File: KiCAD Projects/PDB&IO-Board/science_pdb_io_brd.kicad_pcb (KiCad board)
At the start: 2 copper layers, 124 x 94.6 mm, 40 parts, among them P11 ENCODER_1, P13 LIMIT1_IN, P14 LIMIT2_IN, P15 LIMIT3_IN, P16 ENCODER_3, P17 MOTOR1_PWM, P18 MOTOR2_PWM, P19 MOTOR3_PWM, P2 RPI_HEADER, P20 MOTOR4_PWM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

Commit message: Progress on Main Board
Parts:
- C4: moved to F.Cu
- U1: footprint Housings_SOIC:SOIC-14_3.9x8.7mm_Pitch1.27mm -> Housings_DIP:DIP-14_W7.62mm
- moved R16 104.8 mm to (181.6, 58.4)
- moved D2 104.8 mm to (181.6, 66.0)
- moved D3 104.8 mm to (194.3, 66.0)
- moved R17 104.8 mm to (194.3, 58.4)
- moved P5 72.4 mm to (119.4, 106.7)
- moved P6 72.4 mm to (139.7, 109.2)
- moved P7 72.4 mm to (129.5, 104.1)
- moved P2 70.0 mm to (174.0, 98.4)
- moved P17 55.3 mm to (108.0, 109.2), turned to 90 degrees
- moved R2 49.5 mm to (93.3, 102.2), turned to 90 degrees
- moved P18 45.0 mm to (108.0, 102.9), turned to 90 degrees
- moved R1 44.1 mm to (89.5, 102.2), turned to 90 degrees
- moved P21 43.6 mm to (88.9, 109.2), turned to 270 degrees
- moved P19 36.3 mm to (108.0, 96.5), turned to 90 degrees
- moved P20 30.5 mm to (108.0, 90.2), turned to 90 degrees
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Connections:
- P3 pad 14: Net-(P3-Pad14) -> /MOTOR4_PWM
- P3 pad 16: Net-(P3-Pad16) -> /MOTOR3_PWM
- P4 pad 45: /MOTOR3_PWM -> Net-(P4-Pad45)
- P4 pad 46: /MOTOR4_PWM -> Net-(P4-Pad46)
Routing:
- net /I2C_SDA: track 65.3 -> 184.7 mm
- net /SPI_CLK: track 45.2 -> 158.9 mm
- net /SPI_CS: track 52.5 -> 165.7 mm
- net /SPI_DO: track 51.2 -> 151.5 mm
- net /I2C_SCL: track 89.3 -> 172.4 mm
- net GNDA: track 16.5 -> 82.6 mm
- net /MOISTURE_IN: track 12.5 -> 78.2 mm
- net /MOTOR1_PWM: track 34.3 -> 81.6 mm
- net /MOTOR2_PWM: track 28.4 -> 65.1 mm
- net /B_LIM2: track 40.2 -> 59.1 mm
- net /B_LIM1: track 52.5 -> 70.2 mm
- net /B_LIM3: track 22.9 -> 38.9 mm
- net +3V3: track 0.00 -> 13.9 mm
- net /MOTOR4_PWM: track 22.9 -> 12.6 mm
- net /LIMIT3_IN: track 27.8 -> 33.7 mm
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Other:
- board text added: "+3.3V"
- board text added: "+5V"
- board text added: "3.3V"
- board text added: "A"
- board text added: "A_IN"
- board text added: "B"
- board text added: "BTN"
- board text added: "ENCODER 1"
- board text added: "ENCODER 2"
- board text added: "ENCODER 3"
- board text added: "GND"
- board text added: "LIMSW 1"
- board text added: "LIMSW 2"
- board text added: "LIMSW 3"
- board text added: "MOISTURE"
- board text added: "MOT1 PWM"
- board text added: "MOT2 PWM"
- board text added: "MOT3 PWM"
- board text added: "MOT4 PWM"
- board text added: "PWM"

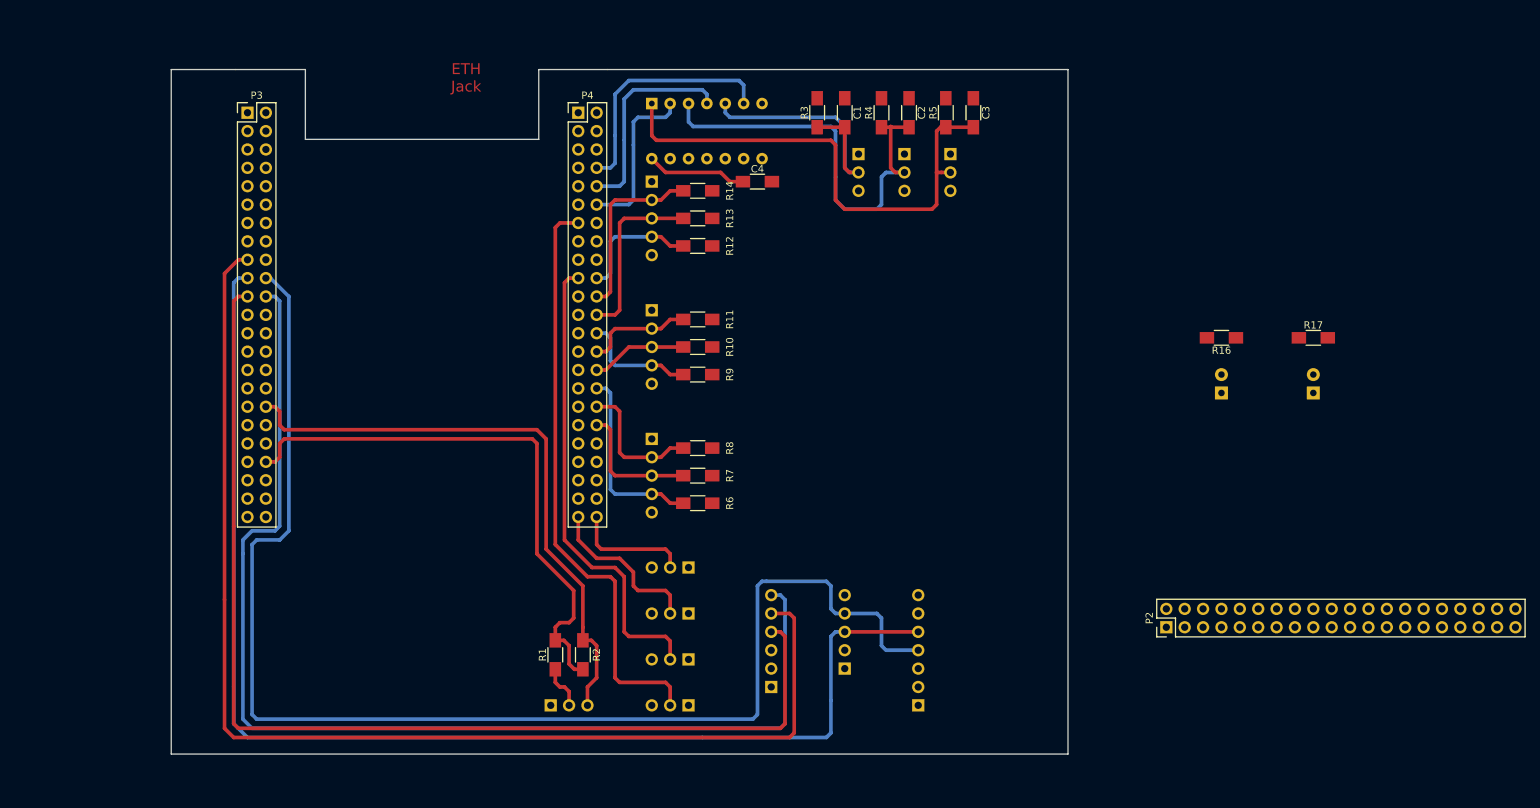
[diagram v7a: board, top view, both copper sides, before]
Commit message: Main Board Layout Mostly Complete
Still needs power routed, but everything else is pretty much finished
now.
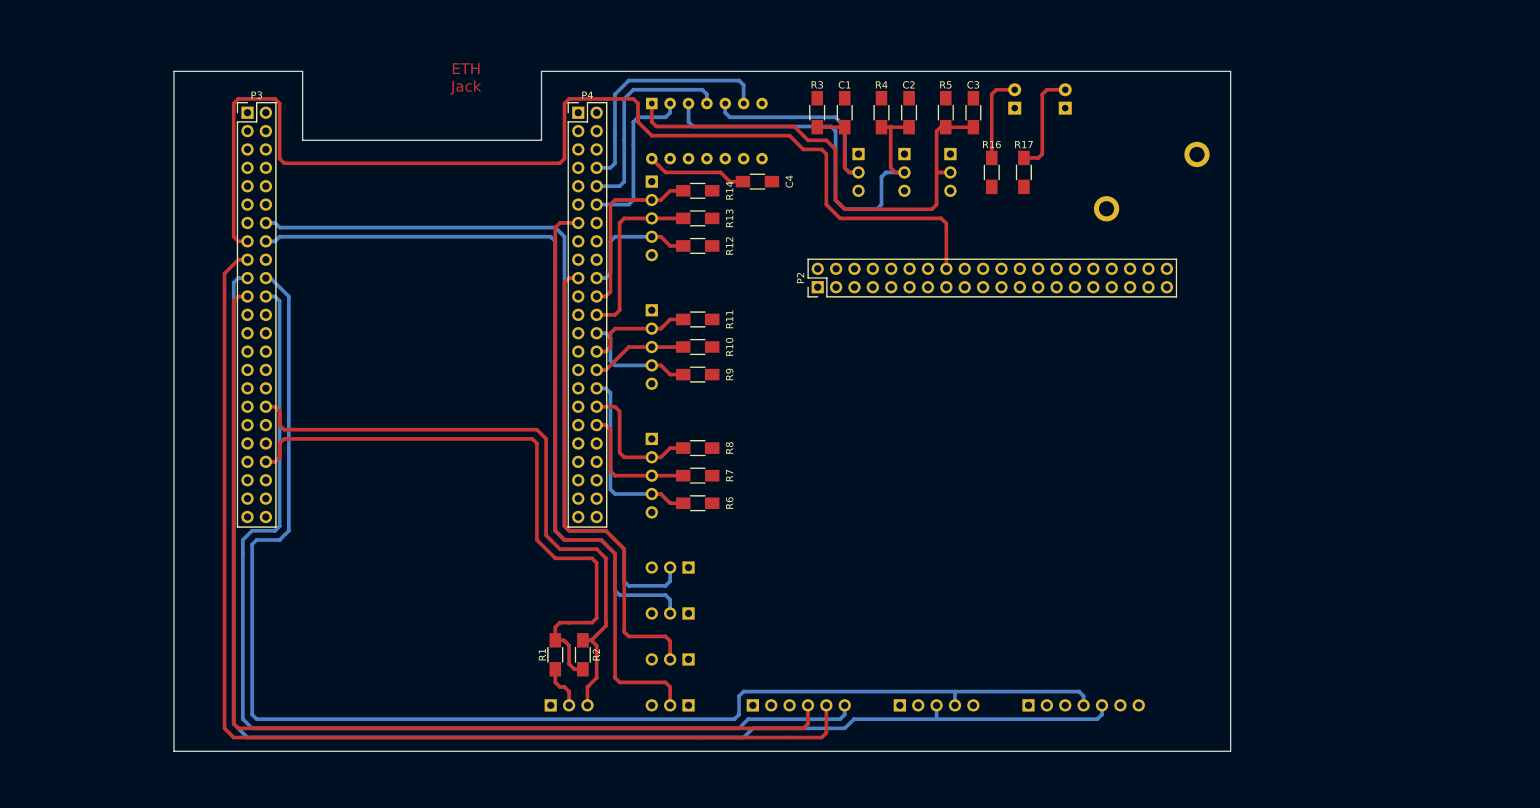
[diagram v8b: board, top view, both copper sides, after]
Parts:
- added P1: PWR_IN, .pretty:PHOENIX_1792229, B.Cu at (157.5, 36.8)
- moved P2 67.3 mm to (125.8, 51.4)
- moved D3 52.2 mm to (160.0, 26.7)
- moved D2 48.6 mm to (153.0, 26.7)
- moved R17 46.1 mm to (154.3, 35.6), turned to 90 degrees
- moved R16 39.1 mm to (149.9, 35.6), turned to 90 degrees
- moved P6 15.2 mm to (154.9, 109.2), turned to 270 degrees
- moved P7 9.16 mm to (137.2, 109.2), turned to 270 degrees
- moved P5 3.59 mm to (116.8, 109.2), turned to 270 degrees
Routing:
- net /CAM_TRIG: track 0.00 -> 154.6 mm
- net /MOTOR4_PWM: track 12.6 -> 104.9 mm
- net /MOTOR3_PWM: track 19.5 -> 105.2 mm
- net /I2C_SCL: track 172.4 -> 188.4 mm
- net Net-(D3-Pad2): track 0.00 -> 14.5 mm
- net Net-(D2-Pad2): track 0.00 -> 12.2 mm
- net /SPI_CS: track 165.7 -> 154.6 mm
- net /SPI_CLK: track 158.9 -> 149.7 mm
- net /SPI_DO: track 151.5 -> 143.0 mm
- net /MOISTURE_IN: track 78.2 -> 85.7 mm
- net GNDA: track 82.6 -> 87.7 mm
- net Net-(P4-Pad46): track 3.81 -> 0.00 mm
- net Net-(P4-Pad45): track 3.17 -> 0.00 mm
- net /I2C_SDA: track 184.7 -> 187.7 mm
- net /B_LIM1: track 70.2 -> 68.7 mm
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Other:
- board size 124 x 94.6 mm -> 146.1 x 94 mm
- board text added: "3.3V Power"
- board text added: "5V"
- board text added: "5V Power"
- board text added: "BeagleBone Black"
- board text added: "I_SCL"
- board text added: "I_SDA"
- board text added: "N/C"
- board text added: "Raspberry Pi 3"
- board text added: "SW_IN"
- board text added: "S_CK"
- board text added: "S_CS"
- board text added: "S_DO"
- board text added: "Sci Main Board v1 UW Husky Robotics Cai B. / Jaden B."
- board text removed: "+3.3V"
- board text removed: "+5V"
